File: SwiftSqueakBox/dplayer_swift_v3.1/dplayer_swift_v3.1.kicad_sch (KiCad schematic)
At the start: 10 parts, among them SW1 Reset, U1 ATtiny85-20P, U2 dfplayer

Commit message: update pcb and schematic
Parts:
- added J2: ADKEY, Connector_PinHeader_2.00mm:PinHeader_1x03_P2.00mm_Vertical, symbol Connector_Generic:Conn_01x03
- added J3: DAC, Connector_PinHeader_2.00mm:PinHeader_1x03_P2.00mm_Vertical, symbol Connector_Generic:Conn_01x03
- renumbered R3 to R1, R1 to R2, R2 to R3, SW1 to SW2
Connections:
- net GND: now also U2.10 (GND), J2.1 (Pin_1), J3.1 (Pin_1)
- new net: J2.3 (Pin_3), U2.12 (ADKEY_1)
- new net: J2.2 (Pin_2), U2.13 (ADKEY_2)
- new net: J3.3 (Pin_3), U2.4 (DAC_R)
- new net: J3.2 (Pin_2), U2.5 (DAC_L)
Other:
- title: Gierzwaluw lokker v3 -> Swift Squeak Box v3.1
- moved on the sheet: C1, D1, LS1, R1, R2, R3, RV1, SW2, U1

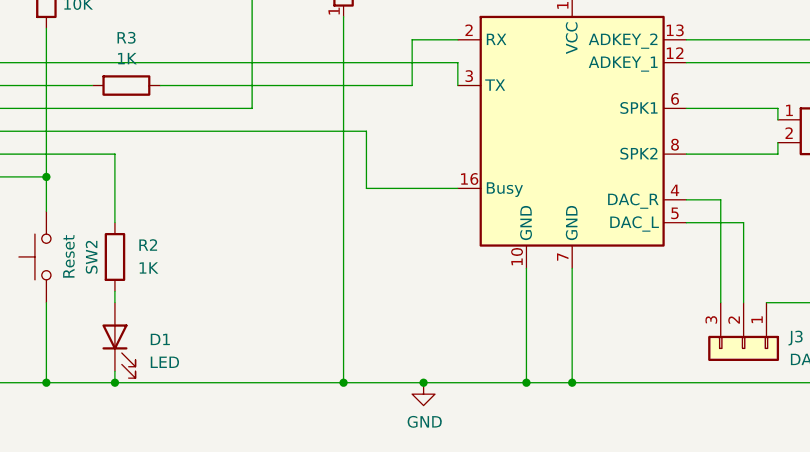
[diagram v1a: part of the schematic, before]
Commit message: Add amplifier, minor update to dplayer pcb
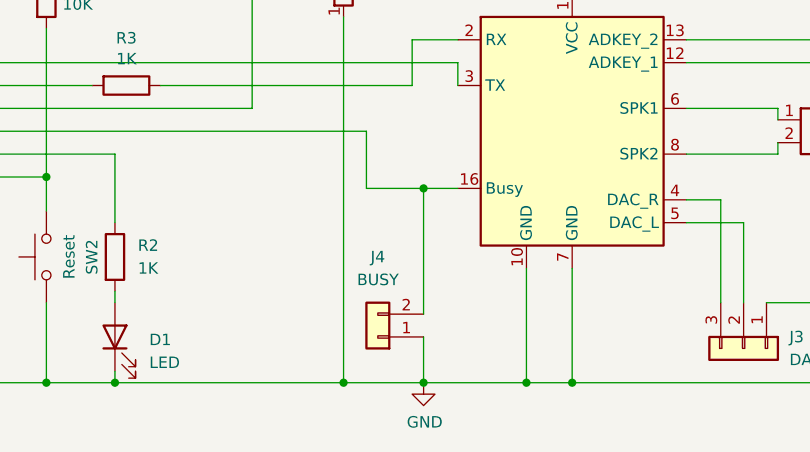
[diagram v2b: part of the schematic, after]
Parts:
- added J4: BUSY, Connector_PinHeader_2.00mm:PinHeader_1x02_P2.00mm_Vertical, symbol Connector_Generic:Conn_01x02
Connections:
- net GND: now also J4.1 (Pin_1)
- net at U1.2 (XTAL1/PB3), U2.16 (Busy): now also J4.2 (Pin_2)
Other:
- title: Swift Squeak Box v3.1 -> Swift Squeak Box v3.1.1
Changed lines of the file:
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@@
   (paper "A4")
   (title_block
-    (title "Swift Squeak Box v3.1")
+    (title "Swift Squeak Box v3.1.1")
   )
   (junction (at 101.6 63.5) (diameter 0) (color 0 0 0 0)
@@
   (junction (at 161.29 115.57) (diameter 0) (color 0 0 0 0)
   )
+  (junction (at 170.18 93.98) (diameter 0) (color 0 0 0 0)
+  )
   (junction (at 101.6 115.57) (diameter 0) (color 0 0 0 0)
   )
@@
     (stroke (width 0) (type default) (color 0 0 0 0))
   )
-  (wire (pts (xy 163.83 93.98) (xy 173.99 93.98))
+  (wire (pts (xy 170.18 107.95) (xy 170.18 93.98))
     (stroke (width 0) (type default) (color 0 0 0 0))
   )
@@
     (stroke (width 0) (type default) (color 0 0 0 0))
   )
+  (wire (pts (xy 163.83 93.98) (xy 170.18 93.98))
+    (stroke (width 0) (type default) (color 0 0 0 0))
+  )
   (wire (pts (xy 151.13 71.12) (xy 151.13 85.09))
     (stroke (width 0) (type default) (color 0 0 0 0))
@@
   )
   (wire (pts (xy 116.84 87.63) (xy 163.83 87.63))
+    (stroke (width 0) (type default) (color 0 0 0 0))
+  )
+  (wire (pts (xy 170.18 93.98) (xy 173.99 93.98))
+    (stroke (width 0) (type default) (color 0 0 0 0))
+  )
+  (wire (pts (xy 170.18 110.49) (xy 170.18 115.57))
     (stroke (width 0) (type default) (color 0 0 0 0))
   )
@@
     (pin "2")
   )
+  (symbol (lib_id "Connector_Generic:Conn_01x02") (at 165.1 110.49 180) (unit 1)
+    (in_bom yes) (on_board yes) (fields_autoplaced)
+    (property "Reference" "J4" (id 0) (at 165.1 101.6 0))
+    (property "Value" "BUSY" (id 1) (at 165.1 104.14 0))
+    (property "Footprint" "Connector_PinHeader_2.00mm:PinHeader_1x02_P2.00mm_Vertical" (id 2) (at 165.1 110.49 0)
+      (effects (font (size 1.27 1.27)) hide)
+    )
+    (property "Datasheet" "~" (id 3) (at 165.1 110.49 0)
+      (effects (font (size 1.27 1.27)) hide)
+    )
+    (pin "1")
+    (pin "2")
+  )
   (symbol (lib_id "Device:C") (at 78.74 77.47 0) (unit 1)
     (in_bom yes) (on_board yes) (fields_autoplaced)
@@
       (reference "J3") (unit 1) (value "DAC") (footprint "Connector_PinHeader_2.00mm:PinHeader_1x03_P2.00mm_Vertical")
     )
+    (path "/229c16f1-6d86-4ca8-81d8-30357072b772"
+      (reference "J4") (unit 1) (value "BUSY") (footprint "Connector_PinHeader_2.00mm:PinHeader_1x02_P2.00mm_Vertical")
+    )
     (path "/00000000-0000-0000-0000-000062922a2a"

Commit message: Update SSB Schematic and pcb V3.1.2
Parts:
- removed LS1: Speaker, Connector_PinHeader_2.00mm:PinHeader_1x02_P2.00mm_Vertical, symbol Device:Speaker
- added J5: LS, Connector_JST:JST_PH_B2B-PH-K_1x02_P2.00mm_Vertical, symbol Connector_Generic:Conn_01x02
- added J6: Power, Connector_JST:JST_PH_B2B-PH-K_1x02_P2.00mm_Vertical, symbol Connector_Generic:Conn_01x02
- added J7: MUTE, Connector_JST:JST_PH_B2B-PH-K_1x02_P2.00mm_Vertical, symbol Connector_Generic:Conn_01x02
- J2, J3: footprint Connector_PinHeader_2.00mm:PinHeader_1x03_P2.00mm_Vertical -> Connector_JST:JST_PH_B3B-PH-K_1x03_P2.00mm_Vertical
- J4: footprint Connector_PinHeader_2.00mm:PinHeader_1x02_P2.00mm_Vertical -> Connector_JST:JST_PH_B2B-PH-K_1x02_P2.00mm_Vertical
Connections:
- net +5V: now also J6.1 (Pin_1)
- net GND: now also J2.3 (Pin_3), J3.3 (Pin_3), J4.2 (Pin_2), J6.2 (Pin_2), J7.2 (Pin_2); no longer J2.1 (Pin_1), J3.1 (Pin_1), J4.1 (Pin_1)
- net at U2.12 (ADKEY_1): now also J2.2 (Pin_2); no longer J2.3 (Pin_3)
- net at U2.13 (ADKEY_2): now also J2.1 (Pin_1); no longer J2.2 (Pin_2)
- net at U1.2 (XTAL1/PB3), U2.16 (Busy): now also J4.1 (Pin_1); no longer J4.2 (Pin_2)
- net at U2.4 (DAC_R): now also J3.1 (Pin_1); no longer J3.3 (Pin_3)
- net at U2.6 (SPK1): now also J5.1 (Pin_1)
- net at U2.8 (SPK2): now also J5.2 (Pin_2)
- net at R2.1, U1.3 (XTAL2/PB4): now also J7.1 (Pin_1)
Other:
- moved on the sheet: J4
